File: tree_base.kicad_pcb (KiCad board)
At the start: 2 copper layers, 61 x 61 mm, 17 parts, among them Q1 DMG2302U, SW1 SW_SPDT, U1 MCP1640BCH

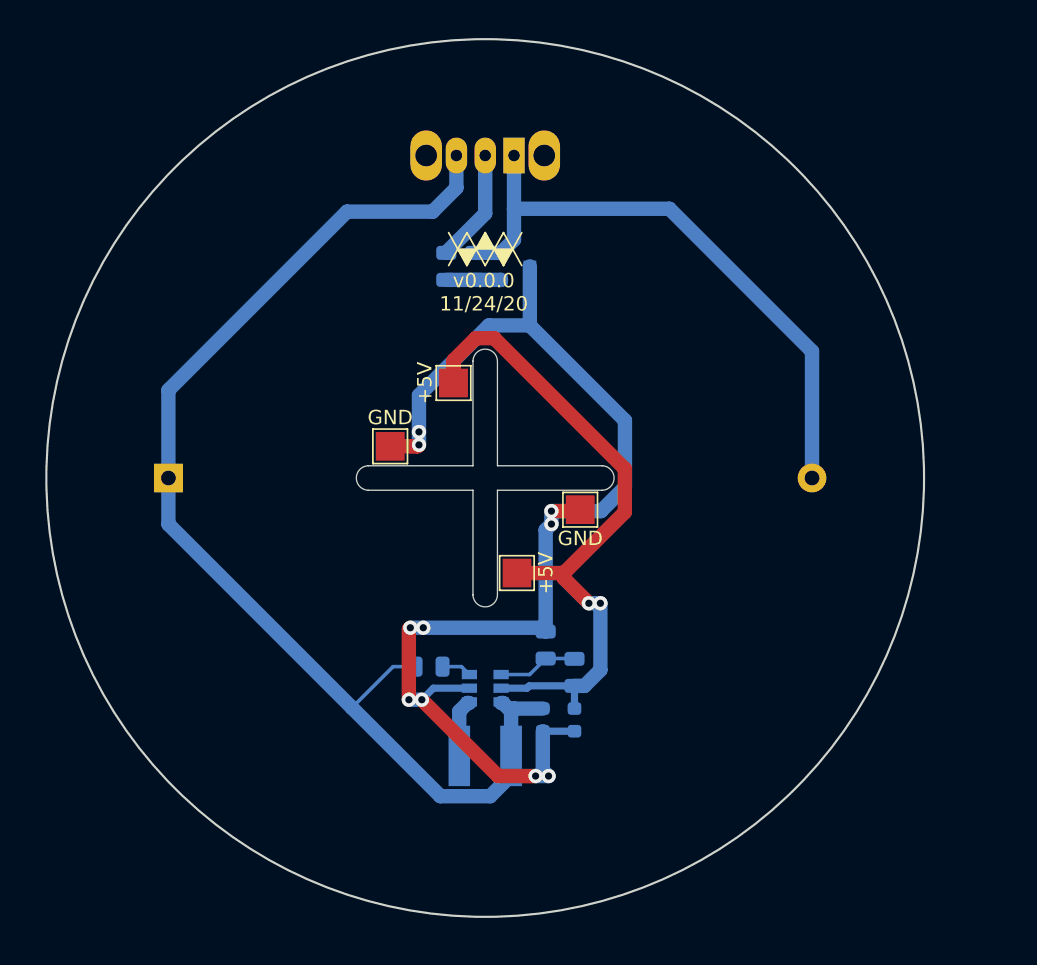
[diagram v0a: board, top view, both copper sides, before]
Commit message: Update with changes to use attiny13a only
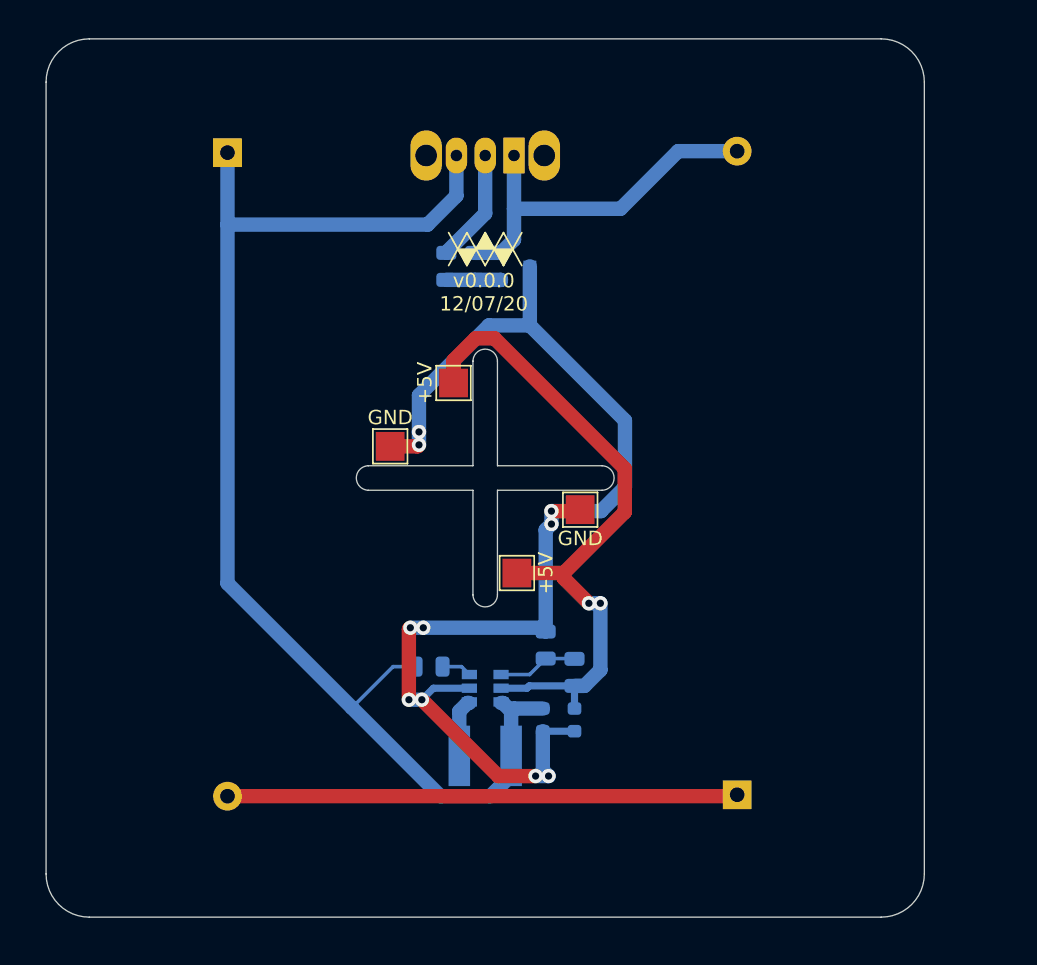
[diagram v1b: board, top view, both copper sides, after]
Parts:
- added BT2: Battery, Battery:BatteryHolder_Keystone_2466_1xAAA, B.Cu at (46.8, 33.6)
- moved BT1 45.2 mm to (82.2, 78.2), turned to 90 degrees
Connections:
- BT1 pad 1: +1-1.5V -> Net-(BT1-Pad1)
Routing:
- net Net-(BT1-Pad1): track 0.00 -> 35.4 mm
- net GND: track 42.5 -> 26.1 mm
- net +1-1.5V: track 82.9 -> 89.1 mm
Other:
- outline, holes or cut-outs redrawn
- board text added: "v0.0.0 12/07/20"
- board text removed: "v0.0.0 11/24/20"

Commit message: Add USB variant; update to use 3xAAA
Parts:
- removed BT2: Battery, Battery:BatteryHolder_Keystone_2466_1xAAA
- BT1: footprint Battery:BatteryHolder_Keystone_2466_1xAAA -> WM_lib:BatteryHolder_Keystone_2479_3xAAA_noscrew
- moved BT1 42.5 mm to (40.9, 68.1), turned to 0 degrees
- moved REF** 24.8 mm to (83.8, 56.1), turned to 270 degrees
- moved Q1 17.9 mm to (50.5, 34.0)
- moved R4 17.9 mm to (45.7, 34.0)
- moved R5 17.9 mm to (47.7, 34.0)
- moved R3 17.3 mm to (58.7, 81.8)
- moved R2 16.2 mm to (61.4, 82.8), turned to 180 degrees
- moved L1 15.1 mm to (50.6, 81.0), turned to 90 degrees
- moved U1 13.9 mm to (55.3, 81.0), turned to 270 degrees
- moved C2 10.7 mm to (66.5, 82.8), turned to 0 degrees
- moved R1 9.27 mm to (57.6, 78.0), turned to 180 degrees
- moved C1 9.12 mm to (61.0, 77.9), turned to 0 degrees
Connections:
- BT1 pad 1: Net-(BT1-Pad1) -> +1-1.5V
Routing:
- net Net-(BT1-Pad1): track 35.4 -> 0.00 mm
- net +5V: track 47.4 -> 76.5 mm, vias 2 -> 1
- net POW_GND: track 85.2 -> 110.3 mm, vias 10 -> 2
- net GND: track 26.1 -> 1.81 mm, vias 0 -> 3
- net +SWV: track 7.88 -> 27.3 mm, vias 0 -> 1
- net +1-1.5V: track 89.1 -> 85.1 mm
- net Net-(R2-Pad2): track 5.57 -> 4.50 mm
- added copper zone on B.Cu, net GND
- added copper zone on F.Cu, net GND
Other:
- board text added: "v0.1.0 12/18/20"
- board text removed: "v0.0.0 12/07/20"
